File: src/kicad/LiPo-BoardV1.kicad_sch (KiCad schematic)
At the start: 26 parts, among them IC1 MT3608, IC2 TP4056, IC3 FS312F-G, J1 MICRO_USB, J2 CON-PAD, J3 CON-PAD, J4 CON-PAD, J5 CON-PAD, Q1 FS8205

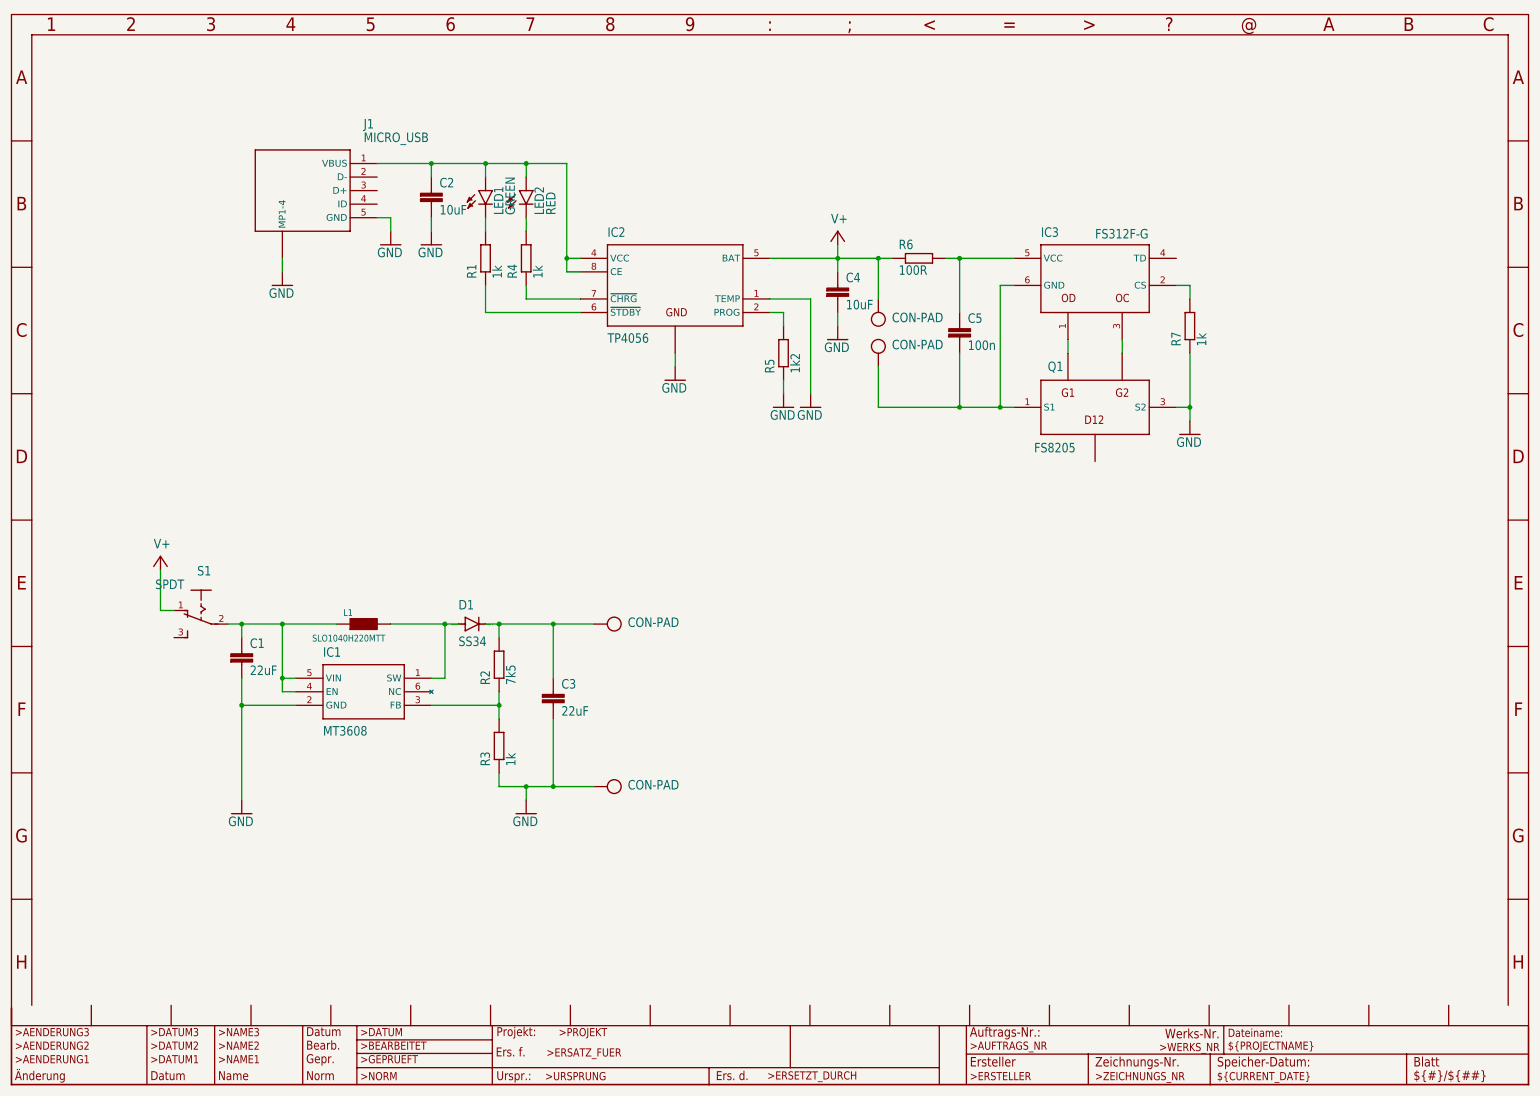
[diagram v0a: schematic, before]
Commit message: Update kicad schematic
make it prettier
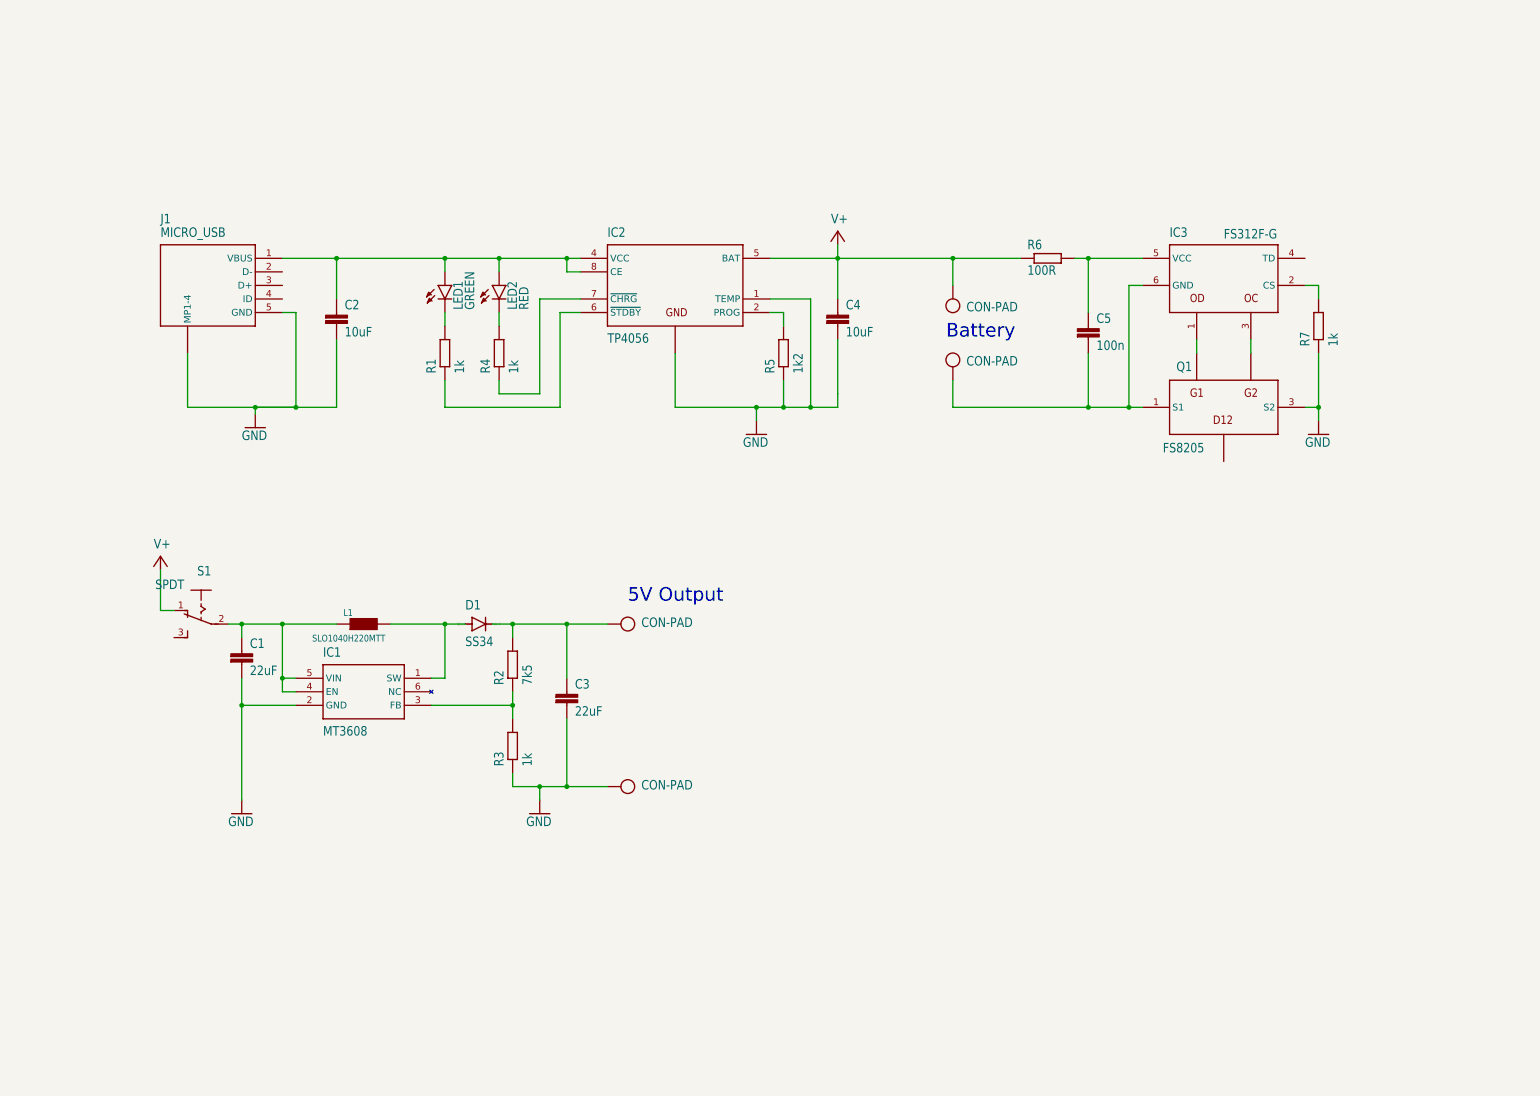
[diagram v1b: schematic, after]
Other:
- note added: "5V Output"
- note added: "Battery"
- company: (none) -> Jakob Holz
- title: (none) -> LiPo-Board
- moved on the sheet: C2, C3, C4, C5, D1, IC3, J1, LED1, LED2, Q1, R1, R2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
